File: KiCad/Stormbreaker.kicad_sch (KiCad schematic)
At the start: 45 parts, among them J1 Micro_SD_Card_Det2, J2 USB_C_Receptacle_USB2.0_14P, J3 Conn_01x03, J4 FAN, Q1 PMOS, Q2 NMOS, SW1 SW_Push, U1 BQ25895RTW, U3 ATtiny1616-M

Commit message: Nearing completion...but no idea how to mount it
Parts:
- removed TP8: SDA, TestPoint:TestPoint_Pad_D1.0mm, symbol Connector:TestPoint
- removed TP9: SCL, TestPoint:TestPoint_Pad_D1.0mm, symbol Connector:TestPoint
- added J5: Conn_01x02, Connector_PinSocket_1.00mm:PinSocket_1x02_P1.00mm_Vertical, symbol Connector_Generic:Conn_01x02
- J2: footprint Connector_USB:USB_C_Receptacle_Amphenol_12401548E4-2A -> Connector_USB:USB_C_Receptacle_GCT_USB4105-xx-A_16P_TopMnt_Horizontal
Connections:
- net SCL: now also J5.2 (Pin_2)
- net SDA: now also J5.1 (Pin_1)
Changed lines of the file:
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@@
 	)
 	(junction
-		(at 201.93 92.71)
-		(diameter 0)
-		(color 0 0 0 0)
-	)
-	(junction
 		(at 62.23 171.45)
 		(diameter 0)
@@
 	)
 	(junction
-		(at 199.39 95.25)
-		(diameter 0)
-		(color 0 0 0 0)
-	)
-	(junction
 		(at 189.23 60.96)
 		(diameter 0)
@@
 	(wire
 		(pts
-			(xy 199.39 95.25) (xy 214.63 95.25)
+			(xy 187.96 95.25) (xy 214.63 95.25)
 		)
 		(stroke
@@
 	(wire
 		(pts
-			(xy 187.96 92.71) (xy 201.93 92.71)
-		)
-		(stroke
-			(width 0)
-			(type default)
-		)
-	)
-	(wire
-		(pts
-			(xy 201.93 91.44) (xy 201.93 92.71)
-		)
-		(stroke
-			(width 0)
-			(type default)
-		)
-	)
-	(wire
-		(pts
 			(xy 80.01 171.45) (xy 77.47 171.45)
 		)
@@
 	(wire
 		(pts
-			(xy 187.96 95.25) (xy 199.39 95.25)
-		)
-		(stroke
-			(width 0)
-			(type default)
-		)
-	)
-	(wire
-		(pts
 			(xy 80.01 158.75) (xy 77.47 158.75)
 		)
@@
 	(wire
 		(pts
-			(xy 199.39 91.44) (xy 199.39 95.25)
-		)
-		(stroke
-			(width 0)
-			(type default)
-		)
-	)
-	(wire
-		(pts
 			(xy 135.89 96.52) (xy 135.89 97.79)
 		)
@@
 	(wire
 		(pts
-			(xy 201.93 92.71) (xy 214.63 92.71)
+			(xy 187.96 92.71) (xy 214.63 92.71)
 		)
 		(stroke
@@
 		)
 	)
+	(global_label "SCL"
+		(shape output)
+		(at 116.84 123.19 0)
+		(fields_autoplaced yes)
+		(effects
+			(font
+				(size 1.27 1.27)
+			)
+			(justify left)
+		)
+		(property "Intersheetrefs" "${INTERSHEET_REFS}"
+			(at 123.3328 123.19 0)
+			(effects
+				(font
+					(size 1.27 1.27)
+				)
+				(justify left)
+				(hide yes)
+			)
+		)
+	)
 	(global_label "SD_D1"
 		(shape bidirectional)
@@
 		)
 	)
+	(global_label "SDA"
+		(shape bidirectional)
+		(at 116.84 125.73 0)
+		(fields_autoplaced yes)
+		(effects
+			(font
+				(size 1.27 1.27)
+			)
+			(justify left)
+		)
+		(property "Intersheetrefs" "${INTERSHEET_REFS}"
+			(at 123.3328 125.73 0)
+			(effects
+				(font
+					(size 1.27 1.27)
+				)
+				(justify left)
+				(hide yes)
+			)
+		)
+	)
 	(global_label "SD_D0"
 		(shape bidirectional)
@@
 	)
 	(symbol
-		(lib_id "Connector:TestPoint")
-		(at 201.93 91.44 0)
-		(mirror y)
-		(unit 1)
-		(exclude_from_sim no)
-		(in_bom yes)
-		(on_board yes)
-		(dnp no)
-		(fields_autoplaced yes)
-		(property "Reference" "TP9"
-			(at 204.47 86.8679 0)
-			(effects
-				(font
-					(size 1.27 1.27)
-				)
-				(justify right)
-			)
-		)
-		(property "Value" "SCL"
-			(at 204.47 89.4079 0)
-			(effects
-				(font
-					(size 1.27 1.27)
-				)
-				(justify right)
-			)
-		)
-		(property "Footprint" "TestPoint:TestPoint_Pad_D1.0mm"
-			(at 196.85 91.44 0)
-			(effects
-				(font
-					(size 1.27 1.27)
-				)
-				(hide yes)
-			)
-		)
-		(property "Datasheet" "~"
-			(at 196.85 91.44 0)
-			(effects
-				(font
-					(size 1.27 1.27)
-				)
-				(hide yes)
-			)
-		)
-		(property "Description" "test point"
-			(at 201.93 91.44 0)
-			(effects
-				(font
-					(size 1.27 1.27)
-				)
-				(hide yes)
-			)
-		)
-		(pin "1"
-		)
-		(instances
-			(project "Stormbreaker"
-				(path "/dcc89f95-4ae4-4756-aa81-33bf4d3c86ca"
-					(reference "TP9")
-					(unit 1)
-				)
-			)
-		)
-	)
-	(symbol
 		(lib_id "Device:C_Small")
 		(at 57.15 160.02 0)
@@
 	)
 	(symbol
-		(lib_id "Connector:TestPoint")
-		(at 199.39 91.44 0)
-		(unit 1)
-		(exclude_from_sim no)
-		(in_bom yes)
-		(on_board yes)
-		(dnp no)
-		(property "Reference" "TP8"
-			(at 196.85 89.4081 0)
-			(effects
-				(font
-					(size 1.27 1.27)
-				)
-				(justify right)
-			)
-		)
-		(property "Value" "SDA"
-			(at 196.85 86.8681 0)
-			(effects
-				(font
-					(size 1.27 1.27)
-				)
-				(justify right)
-			)
-		)
-		(property "Footprint" "TestPoint:TestPoint_Pad_D1.0mm"
-			(at 204.47 91.44 0)
-			(effects
-				(font
-					(size 1.27 1.27)
-				)
-				(hide yes)
-			)
-		)
-		(property "Datasheet" "~"
-			(at 204.47 91.44 0)
-			(effects
-				(font
-					(size 1.27 1.27)
-				)
-				(hide yes)
-			)
-		)
-		(property "Description" "test point"
-			(at 199.39 91.44 0)
-			(effects
-				(font
-					(size 1.27 1.27)
-				)
-				(hide yes)
-			)
-		)
-		(pin "1"
-		)
-		(instances
-			(project "Stormbreaker"
-				(path "/dcc89f95-4ae4-4756-aa81-33bf4d3c86ca"
-					(reference "TP8")
-					(unit 1)
-				)
-			)
-		)
-	)
-	(symbol
 		(lib_id "Device:C_Small")
 		(at 133.35 158.75 0)
@@
 			)
 		)
-		(property "Footprint" "Connector_USB:USB_C_Receptacle_Amphenol_12401548E4-2A"
+		(property "Footprint" "Connector_USB:USB_C_Receptacle_GCT_USB4105-xx-A_16P_TopMnt_Horizontal"
 			(at 269.24 35.56 0)
 			(effects
@@
 					(unit 1)
 				)
+			)
+		)
+	)
+	(symbol
+		(lib_id "Connector_Generic:Conn_01x02")
+		(at 111.76 125.73 180)
+		(unit 1)
+		(exclude_from_sim no)
+		(in_bom yes)
+		(on_board yes)
+		(dnp no)
+		(fields_autoplaced yes)
+		(property "Reference" "J5"
+			(at 111.76 116.84 0)
+			(effects
+				(font
+					(size 1.27 1.27)
+				)
+			)
+		)
+		(property "Value" "Conn_01x02"
+			(at 111.76 119.38 0)
+			(effects
+				(font
+					(size 1.27 1.27)
+				)
+			)
+		)
+		(property "Footprint" "Connector_PinSocket_1.00mm:PinSocket_1x02_P1.00mm_Vertical"
+			(at 111.76 125.73 0)
+			(effects
+				(font
+					(size 1.27 1.27)
+				)
+				(hide yes)
+			)
+		)
+		(property "Datasheet" "~"
+			(at 111.76 125.73 0)
+			(effects
+				(font
+					(size 1.27 1.27)
+				)
+				(hide yes)
+			)
+		)
+		(property "Description" "Generic connector, single row, 01x02, script generated (kicad-library-utils/schlib/autogen/connector/)"
+			(at 111.76 125.73 0)
+			(effects
+				(font
+					(size 1.27 1.27)
+				)
+				(hide yes)
+			)
+		)
+		(pin "2"
+		)
+		(pin "1"
+		)
+		(instances
+			(project ""
+				(path "/dcc89f95-4ae4-4756-aa81-33bf4d3c86ca"
+					(reference "J5")
+					(unit 1)
+				)

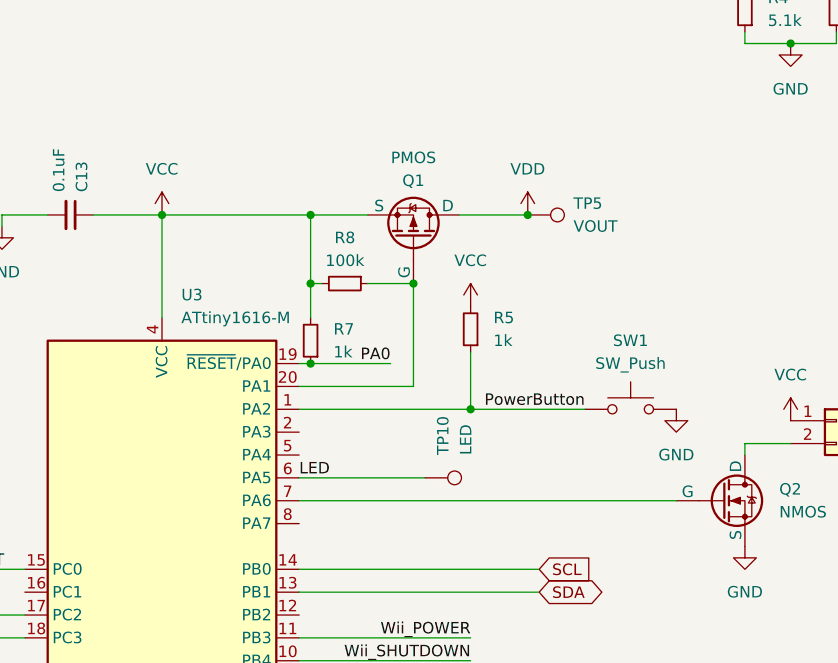
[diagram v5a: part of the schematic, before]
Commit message: Firmware development, minor hardware changes
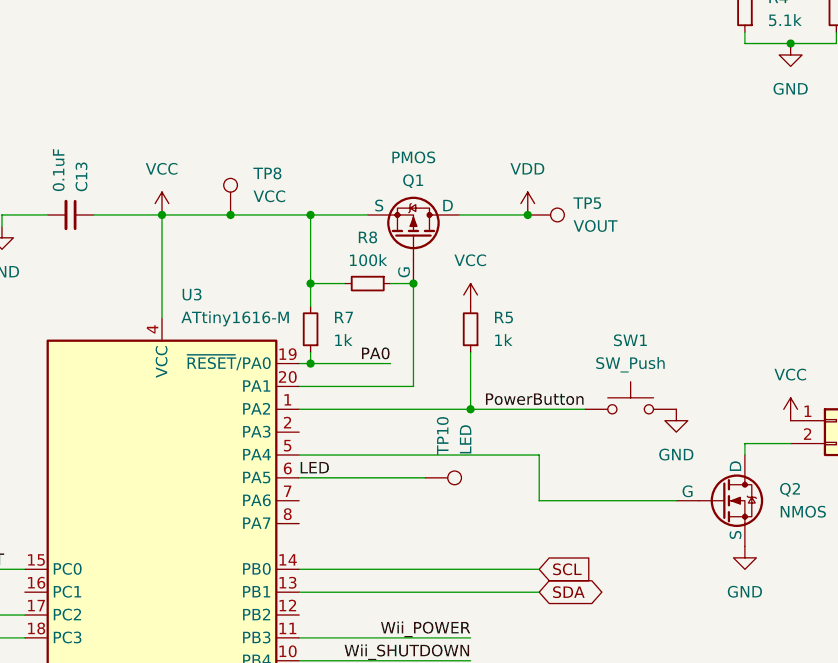
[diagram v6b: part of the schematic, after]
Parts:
- added TP8: VCC, TestPoint:TestPoint_Pad_D2.0mm, symbol Connector:TestPoint
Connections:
- net VCC: now also TP8.1
- net at U3.5 (PA4): now also Q2.1 (G)
- net at U3.7 (PA6): no longer Q2.1 (G)
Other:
- moved on the sheet: R7, R8
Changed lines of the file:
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@@
 	)
 	(junction
+		(at 180.34 53.34)
+		(diameter 0)
+		(color 0 0 0 0)
+	)
+	(junction
 		(at 242.57 34.29)
 		(diameter 0)
@@
 	(wire
 		(pts
+			(xy 214.63 80.01) (xy 214.63 85.09)
+		)
+		(stroke
+			(width 0)
+			(type default)
+		)
+	)
+	(wire
+		(pts
 			(xy 189.23 53.34) (xy 189.23 60.96)
 		)
@@
 	(wire
 		(pts
+			(xy 189.23 68.58) (xy 189.23 69.85)
+		)
+		(stroke
+			(width 0)
+			(type default)
+		)
+	)
+	(wire
+		(pts
 			(xy 106.68 95.25) (xy 97.79 95.25)
 		)
@@
 	(wire
 		(pts
-			(xy 195.58 60.96) (xy 200.66 60.96)
+			(xy 198.12 60.96) (xy 200.66 60.96)
 		)
 		(stroke
@@
 	(wire
 		(pts
-			(xy 189.23 60.96) (xy 189.23 64.77)
+			(xy 189.23 60.96) (xy 189.23 63.5)
 		)
 		(stroke
@@
 	(wire
 		(pts
+			(xy 214.63 85.09) (xy 229.87 85.09)
+		)
+		(stroke
+			(width 0)
+			(type default)
+		)
+	)
+	(wire
+		(pts
 			(xy 113.03 154.94) (xy 133.35 154.94)
 		)
@@
 	(wire
 		(pts
-			(xy 172.72 53.34) (xy 189.23 53.34)
+			(xy 172.72 53.34) (xy 180.34 53.34)
 		)
 		(stroke
@@
 	(wire
 		(pts
+			(xy 187.96 80.01) (xy 214.63 80.01)
+		)
+		(stroke
+			(width 0)
+			(type default)
+		)
+	)
+	(wire
+		(pts
 			(xy 247.65 27.94) (xy 257.81 27.94)
 		)
@@
 	(wire
 		(pts
-			(xy 189.23 60.96) (xy 190.5 60.96)
+			(xy 180.34 53.34) (xy 189.23 53.34)
 		)
 		(stroke
@@
 	(wire
 		(pts
-			(xy 229.87 85.09) (xy 187.96 85.09)
+			(xy 189.23 60.96) (xy 193.04 60.96)
 		)
 		(stroke
@@
 	(symbol
 		(lib_id "Device:R_Small")
-		(at 189.23 67.31 180)
+		(at 189.23 66.04 180)
 		(unit 1)
 		(exclude_from_sim no)
@@
 		(fields_autoplaced yes)
 		(property "Reference" "R7"
-			(at 191.77 66.0399 0)
+			(at 191.77 64.7699 0)
 			(effects
 				(font
@@
 		)
 		(property "Value" "1k"
-			(at 191.77 68.5799 0)
+			(at 191.77 67.3099 0)
 			(effects
 				(font
@@
 		)
 		(property "Footprint" "Resistor_SMD:R_0603_1608Metric"
-			(at 189.23 67.31 0)
+			(at 189.23 66.04 0)
 			(effects
 				(font
@@
 		)
 		(property "Datasheet" "~"
-			(at 189.23 67.31 0)
+			(at 189.23 66.04 0)
 			(effects
 				(font
@@
 		)
 		(property "Description" "Resistor, small symbol"
-			(at 189.23 67.31 0)
+			(at 189.23 66.04 0)
 			(effects
 				(font
@@
 	)
 	(symbol
+		(lib_id "Connector:TestPoint")
+		(at 180.34 53.34 0)
+		(unit 1)
+		(exclude_from_sim no)
+		(in_bom yes)
+		(on_board yes)
+		(dnp no)
+		(fields_autoplaced yes)
+		(property "Reference" "TP8"
+			(at 182.88 48.7679 0)
+			(effects
+				(font
+					(size 1.27 1.27)
+				)
+				(justify left)
+			)
+		)
+		(property "Value" "VCC"
+			(at 182.88 51.3079 0)
+			(effects
+				(font
+					(size 1.27 1.27)
+				)
+				(justify left)
+			)
+		)
+		(property "Footprint" "TestPoint:TestPoint_Pad_D2.0mm"
+			(at 185.42 53.34 0)
+			(effects
+				(font
+					(size 1.27 1.27)
+				)
+				(hide yes)
+			)
+		)
+		(property "Datasheet" "~"
+			(at 185.42 53.34 0)
+			(effects
+				(font
+					(size 1.27 1.27)
+				)
+				(hide yes)
+			)
+		)
+		(property "Description" "test point"
+			(at 180.34 53.34 0)
+			(effects
+				(font
+					(size 1.27 1.27)
+				)
+				(hide yes)
+			)
+		)
+		(pin "1"
+		)
+		(instances
+			(project "Stormbreaker"
+				(path "/dcc89f95-4ae4-4756-aa81-33bf4d3c86ca"
+					(reference "TP8")
+					(unit 1)
+				)
+			)
+		)
+	)
+	(symbol
 		(lib_id "Device:R_Small")
 		(at 247.65 30.48 180)
@@
 	(symbol
 		(lib_id "Device:R_Small")
-		(at 193.04 60.96 270)
+		(at 195.58 60.96 270)
 		(unit 1)
 		(exclude_from_sim no)
@@
 		(fields_autoplaced yes)
 		(property "Reference" "R8"
-			(at 193.04 55.88 90)
+			(at 195.58 55.88 90)
 			(effects
 				(font
@@
 		)
 		(property "Value" "100k"
-			(at 193.04 58.42 90)
+			(at 195.58 58.42 90)
 			(effects
 				(font
@@
 		)
 		(property "Footprint" "Resistor_SMD:R_0603_1608Metric"
-			(at 193.04 60.96 0)
+			(at 195.58 60.96 0)
 			(effects
 				(font
@@
 		)
 		(property "Datasheet" "~"
-			(at 193.04 60.96 0)
+			(at 195.58 60.96 0)
 			(effects
 				(font
@@
 		)
 		(property "Description" "Resistor, small symbol"
-			(at 193.04 60.96 0)
+			(at 195.58 60.96 0)
 			(effects
 				(font

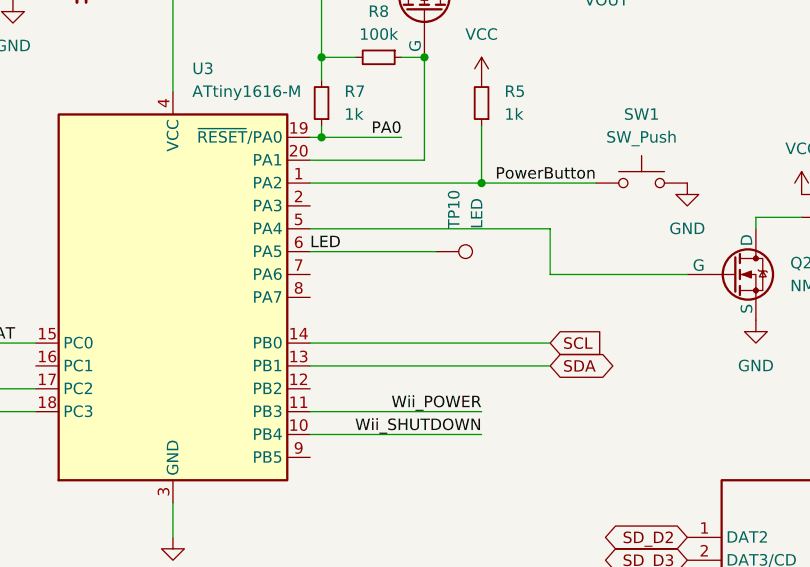
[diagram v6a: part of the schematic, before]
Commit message: Begin interface code, implement safety features
Now loads (and writes) various settings from (and to) EEPROM. Added error handling, to an extent. Added comments for easier understanding. Emergency power-off and shipping mode in over-temp situations. Added ALERT pin for over-temp situations to PCB.
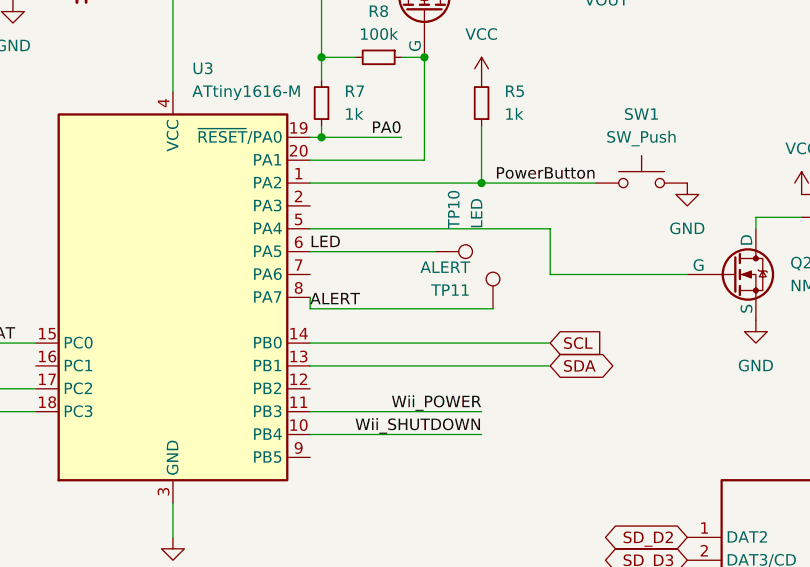
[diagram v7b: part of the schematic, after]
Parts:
- added TP11: ALERT, TestPoint:TestPoint_Pad_D1.0mm, symbol Connector:TestPoint
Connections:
- net ALERT: now reaches U3.8 (PA7)
- net ALERT: now also TP11.1
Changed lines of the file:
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@@
 	(wire
 		(pts
+			(xy 208.28 88.9) (xy 187.96 88.9)
+		)
+		(stroke
+			(width 0)
+			(type default)
+		)
+	)
+	(wire
+		(pts
 			(xy 154.94 53.34) (xy 160.02 53.34)
 		)
@@
 	(wire
 		(pts
+			(xy 187.96 88.9) (xy 187.96 87.63)
+		)
+		(stroke
+			(width 0)
+			(type default)
+		)
+	)
+	(wire
+		(pts
 			(xy 133.35 100.33) (xy 143.51 100.33)
 		)
@@
 		)
 	)
+	(label "ALERT"
+		(at 187.96 88.9 0)
+		(effects
+			(font
+				(size 1.27 1.27)
+			)
+			(justify left bottom)
+		)
+	)
 	(label "PA0"
 		(at 198.12 69.85 180)
@@
 					(unit 1)
 				)
+			)
+		)
+	)
+	(symbol
+		(lib_id "Connector:TestPoint")
+		(at 208.28 88.9 0)
+		(unit 1)
+		(exclude_from_sim no)
+		(in_bom yes)
+		(on_board yes)
+		(dnp no)
+		(property "Reference" "TP11"
+			(at 205.74 86.8681 0)
+			(effects
+				(font
+					(size 1.27 1.27)
+				)
+				(justify right)
+			)
+		)
+		(property "Value" "ALERT"
+			(at 205.74 84.3281 0)
+			(effects
+				(font
+					(size 1.27 1.27)
+				)
+				(justify right)
+			)
+		)
+		(property "Footprint" "TestPoint:TestPoint_Pad_D1.0mm"
+			(at 213.36 88.9 0)
+			(effects
+				(font
+					(size 1.27 1.27)
+				)
+				(hide yes)
+			)
+		)
+		(property "Datasheet" "~"
+			(at 213.36 88.9 0)
+			(effects
+				(font
+					(size 1.27 1.27)
+				)
+				(hide yes)
+			)
+		)
+		(property "Description" "test point"
+			(at 208.28 88.9 0)
+			(effects
+				(font
+					(size 1.27 1.27)
+				)
+				(hide yes)
+			)
+		)
+		(pin "1"
+		)
+		(instances
+			(project "Stormbreaker"
+				(path "/dcc89f95-4ae4-4756-aa81-33bf4d3c86ca"
+					(reference "TP11")
+					(unit 1)
+				)

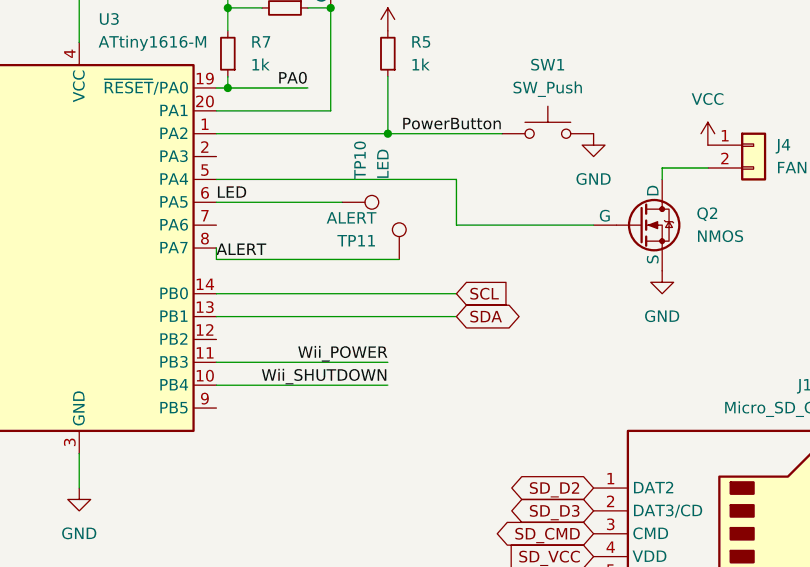
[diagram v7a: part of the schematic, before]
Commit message: Modify fan pin, implement fan control, misc
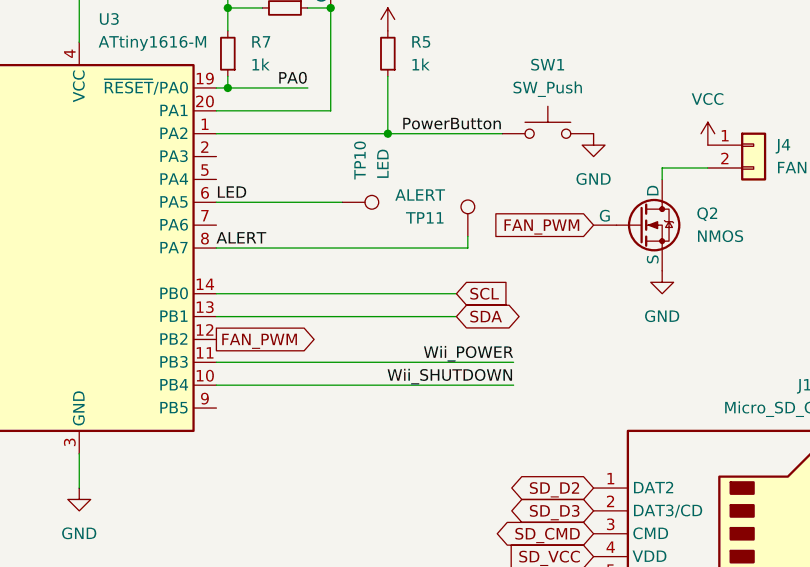
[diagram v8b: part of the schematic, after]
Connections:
- net FAN_PWM: now reaches U3.12 (PB2)
- net FAN_PWM: now also Q2.1 (G)
- net at U3.5 (PA4): no longer Q2.1 (G)
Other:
- moved on the sheet: TP11
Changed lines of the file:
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@@
 	(wire
 		(pts
-			(xy 214.63 80.01) (xy 214.63 85.09)
-		)
-		(stroke
-			(width 0)
-			(type default)
-		)
-	)
-	(wire
-		(pts
 			(xy 189.23 53.34) (xy 189.23 60.96)
 		)
@@
 	(wire
 		(pts
+			(xy 215.9 87.63) (xy 215.9 86.36)
+		)
+		(stroke
+			(width 0)
+			(type default)
+		)
+	)
+	(wire
+		(pts
 			(xy 148.59 152.4) (xy 148.59 153.67)
 		)
@@
 	(wire
 		(pts
-			(xy 208.28 88.9) (xy 187.96 88.9)
+			(xy 215.9 87.63) (xy 187.96 87.63)
 		)
 		(stroke
@@
 	(wire
 		(pts
-			(xy 214.63 85.09) (xy 229.87 85.09)
-		)
-		(stroke
-			(width 0)
-			(type default)
-		)
-	)
-	(wire
-		(pts
 			(xy 113.03 154.94) (xy 133.35 154.94)
 		)
@@
 	(wire
 		(pts
-			(xy 187.96 100.33) (xy 207.01 100.33)
+			(xy 187.96 100.33) (xy 220.98 100.33)
 		)
 		(stroke
@@
 	(wire
 		(pts
-			(xy 187.96 88.9) (xy 187.96 87.63)
-		)
-		(stroke
-			(width 0)
-			(type default)
-		)
-	)
-	(wire
-		(pts
 			(xy 133.35 100.33) (xy 143.51 100.33)
 		)
@@
 	(wire
 		(pts
-			(xy 187.96 80.01) (xy 214.63 80.01)
-		)
-		(stroke
-			(width 0)
-			(type default)
-		)
-	)
-	(wire
-		(pts
 			(xy 247.65 27.94) (xy 257.81 27.94)
 		)
@@
 	(wire
 		(pts
-			(xy 187.96 102.87) (xy 207.01 102.87)
+			(xy 187.96 102.87) (xy 220.98 102.87)
 		)
 		(stroke
@@
 	)
 	(label "ALERT"
-		(at 187.96 88.9 0)
+		(at 187.96 87.63 0)
 		(effects
 			(font
@@
 	)
 	(label "Wii_SHUTDOWN"
-		(at 207.01 102.87 180)
+		(at 220.98 102.87 180)
 		(effects
 			(font
@@
 	)
 	(label "Wii_POWER"
-		(at 207.01 100.33 180)
+		(at 220.98 100.33 180)
 		(effects
 			(font
@@
 		)
 	)
+	(global_label "FAN_PWM"
+		(shape output)
+		(at 187.96 97.79 0)
+		(fields_autoplaced yes)
+		(effects
+			(font
+				(size 1.27 1.27)
+			)
+			(justify left)
+		)
+		(property "Intersheetrefs" "${INTERSHEET_REFS}"
+			(at 199.5933 97.79 0)
+			(effects
+				(font
+					(size 1.27 1.27)
+				)
+				(justify left)
+				(hide yes)
+			)
+		)
+	)
 	(global_label "SD_D0"
 		(shape bidirectional)
@@
 		)
 	)
+	(global_label "FAN_PWM"
+		(shape input)
+		(at 229.87 85.09 180)
+		(fields_autoplaced yes)
+		(effects
+			(font
+				(size 1.27 1.27)
+			)
+			(justify right)
+		)
+		(property "Intersheetrefs" "${INTERSHEET_REFS}"
+			(at 218.2367 85.09 0)
+			(effects
+				(font
+					(size 1.27 1.27)
+				)
+				(justify right)
+				(hide yes)
+			)
+		)
+	)
 	(global_label "SCL_2"
 		(shape input)
@@
 	(symbol
 		(lib_id "Connector:TestPoint")
-		(at 208.28 88.9 0)
+		(at 215.9 86.36 0)
 		(unit 1)
 		(exclude_from_sim no)
@@
 		(dnp no)
 		(property "Reference" "TP11"
-			(at 205.74 86.8681 0)
+			(at 213.36 84.3281 0)
 			(effects
 				(font
@@
 		)
 		(property "Value" "ALERT"
-			(at 205.74 84.3281 0)
+			(at 213.36 81.7881 0)
 			(effects
 				(font
@@
 		)
 		(property "Footprint" "TestPoint:TestPoint_Pad_D1.0mm"
-			(at 213.36 88.9 0)
+			(at 220.98 86.36 0)
 			(effects
 				(font
@@
 		)
 		(property "Datasheet" "~"
-			(at 213.36 88.9 0)
+			(at 220.98 86.36 0)
 			(effects
 				(font
@@
 		)
 		(property "Description" "test point"
-			(at 208.28 88.9 0)
+			(at 215.9 86.36 0)
 			(effects
 				(font
